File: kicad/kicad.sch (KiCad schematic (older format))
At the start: 10 parts, among them J1 Conn_ARM_JTAG_SWD_10, U1 ATSAMC21N18A-TQFP32

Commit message: Added the potentiometer to the schematic
Changed the schematic to reflect the use of the
ADC, PWM and potentiometer.
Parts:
- added RV1: 10K, symbol Device:R_POT
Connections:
- net GND: now also U1.6 (PA05), RV1.3
- net VCC: now also U1.4 (PA03), RV1.1
- net at U1.16 (PA15): now also D1.2 (A)
- net at U1.21 (PA22): no longer D1.2 (A)
- net at U1.3 (PA02): now also RV1.2
- no-connect marks 25 -> 22
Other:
- moved on the sheet: J1, R1
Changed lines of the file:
@@
 L Device:R R1
 U 1 1 5E23DDA0
-P 3900 2550
-F 0 "R1" H 3970 2596 50  0000 L CNN
-F 1 "1K" H 3970 2505 50  0000 L CNN
-F 2 "" V 3830 2550 50  0001 C CNN
-F 3 "~" H 3900 2550 50  0001 C CNN
-	1    3900 2550
-	1    0    0    -1
-$EndComp
-Wire Wire Line
-	3900 4500 4475 4500
+P 3500 2550
+F 0 "R1" H 3570 2596 50  0000 L CNN
+F 1 "1K" H 3570 2505 50  0000 L CNN
+F 2 "" V 3430 2550 50  0001 C CNN
+F 3 "~" H 3500 2550 50  0001 C CNN
+	1    3500 2550
+	1    0    0    -1
+$EndComp
+Wire Wire Line
+	3500 4500 4475 4500
 Connection ~ 5675 1975
 $Comp
@@
 $EndComp
 Wire Wire Line
-	3900 2400 3900 1975
-Wire Wire Line
-	3900 2700 3900 4200
-Wire Wire Line
-	2975 4000 3450 4000
-Wire Wire Line
-	3450 4000 3450 4600
-Wire Wire Line
-	3450 4600 4475 4600
-Wire Wire Line
-	2975 4200 3900 4200
-Connection ~ 3900 4200
-Wire Wire Line
-	3900 4200 3900 4500
-Wire Wire Line
-	4475 4400 3275 4400
-Wire Wire Line
-	3275 4400 3275 4300
-Wire Wire Line
-	3275 4300 2975 4300
-NoConn ~ 2975 4400
+	3500 2400 3500 1975
+Wire Wire Line
+	3500 2700 3500 4300
+Wire Wire Line
+	2975 4100 3175 4100
+Wire Wire Line
+	3175 4100 3175 4600
+Wire Wire Line
+	3175 4600 4475 4600
+Wire Wire Line
+	2975 4300 3500 4300
+Connection ~ 3500 4300
+Wire Wire Line
+	3500 4300 3500 4500
 NoConn ~ 2975 4500
+NoConn ~ 2975 4600
 $Comp
 L local_syms:Conn_ARM_JTAG_SWD_10 J1
 U 1 1 5E24CFFF
-P 2475 4300
-F 0 "J1" H 2525 5081 50  0000 C CNN
-F 1 "Conn_ARM_JTAG_SWD_10" H 2525 4990 50  0000 C CNN
-F 2 "" H 2475 4300 50  0001 C CNN
-F 3 "http://infocenter.arm.com/help/topic/com.arm.doc.ddi0314h/DDI0314H_coresight_components_trm.pdf" V 2125 3050 50  0001 C CNN
-	1    2475 4300
+P 2475 4400
+F 0 "J1" H 2525 5181 50  0000 C CNN
+F 1 "Conn_ARM_JTAG_SWD_10" H 2525 5090 50  0000 C CNN
+F 2 "" H 2475 4400 50  0001 C CNN
+F 3 "http://infocenter.arm.com/help/topic/com.arm.doc.ddi0314h/DDI0314H_coresight_components_trm.pdf" V 2125 3150 50  0001 C CNN
+	1    2475 4400
 	1    0    0    -1
 $EndComp
@@
 	5425 5050 5125 5050
 Wire Wire Line
-	2375 5050 2375 4900
-Wire Wire Line
-	2475 4900 2475 5050
+	2375 5050 2375 5000
+Wire Wire Line
+	2475 5000 2475 5050
 Connection ~ 2475 5050
 Wire Wire Line
 	2475 5050 2375 5050
 Wire Wire Line
-	2575 4900 2575 5050
+	2575 5000 2575 5050
 Connection ~ 2575 5050
 Wire Wire Line
@@
 Connection ~ 5125 5050
 Wire Wire Line
-	5125 5050 2575 5050
+	5125 5050 4325 5050
 $Comp
 L Device:LED D1
@@
 	0    -1   -1   0
 $EndComp
-Wire Wire Line
-	6475 4100 6950 4100
-Wire Wire Line
-	6950 4100 6950 4300
 Wire Wire Line
 	5675 1975 5675 2200
@@
 Connection ~ 5425 1975
 Wire Wire Line
-	5425 1975 3900 1975
+	5425 1975 4325 1975
 Wire Wire Line
 	5425 1975 5675 1975
@@
 	5675 2500 5675 2900
 Wire Wire Line
-	2475 1975 3900 1975
-Wire Wire Line
-	2475 1975 2475 3700
-Connection ~ 3900 1975
+	2475 1975 3500 1975
+Wire Wire Line
+	2475 1975 2475 3800
+Connection ~ 3500 1975
 $Comp
 L Device:C C5
@@
 NoConn ~ 4475 3300
 NoConn ~ 4475 3400
-NoConn ~ 4475 3500
-NoConn ~ 4475 3600
 NoConn ~ 4475 3700
-NoConn ~ 4475 3800
 NoConn ~ 4475 3900
 NoConn ~ 4475 4000
@@
 NoConn ~ 6475 3400
 NoConn ~ 6475 3500
-NoConn ~ 6475 3600
-NoConn ~ 6475 3700
 NoConn ~ 6475 3800
 NoConn ~ 6475 3900
@@
 NoConn ~ 6475 4500
 NoConn ~ 6475 4600
+NoConn ~ 6475 4100
+Wire Wire Line
+	2975 4400 4475 4400
+$Comp
+L Device:R_POT RV1
+U 1 1 5E28D798
+P 3975 3500
+F 0 "RV1" H 3906 3546 50  0000 R CNN
+F 1 "10K" H 3906 3455 50  0000 R CNN
+F 2 "" H 3975 3500 50  0001 C CNN
+F 3 "~" H 3975 3500 50  0001 C CNN
+	1    3975 3500
+	1    0    0    -1
+$EndComp
+Wire Wire Line
+	4125 3500 4475 3500
+Wire Wire Line
+	3975 3350 3975 1975
+Connection ~ 3975 1975
+Wire Wire Line
+	3975 1975 3500 1975
+Wire Wire Line
+	3975 3650 3975 5050
+Connection ~ 3975 5050
+Wire Wire Line
+	3975 5050 2575 5050
+Wire Wire Line
+	4475 3800 4325 3800
+Wire Wire Line
+	4325 3800 4325 5050
+Connection ~ 4325 5050
+Wire Wire Line
+	4325 5050 3975 5050
+Text Label 4325 4325 1    50   ~ 0
+MUXNEG_AIN5
+Wire Wire Line
+	4475 3600 4325 3600
+Wire Wire Line
+	4325 3600 4325 1975
+Connection ~ 4325 1975
+Wire Wire Line
+	4325 1975 3975 1975
+Text Label 4325 3325 1    50   ~ 0
+VREFP_AIN1
+Wire Wire Line
+	6950 3600 6475 3600
+Wire Wire Line
+	6950 3600 6950 4300
+NoConn ~ 6475 3700
 $EndSCHEMATC

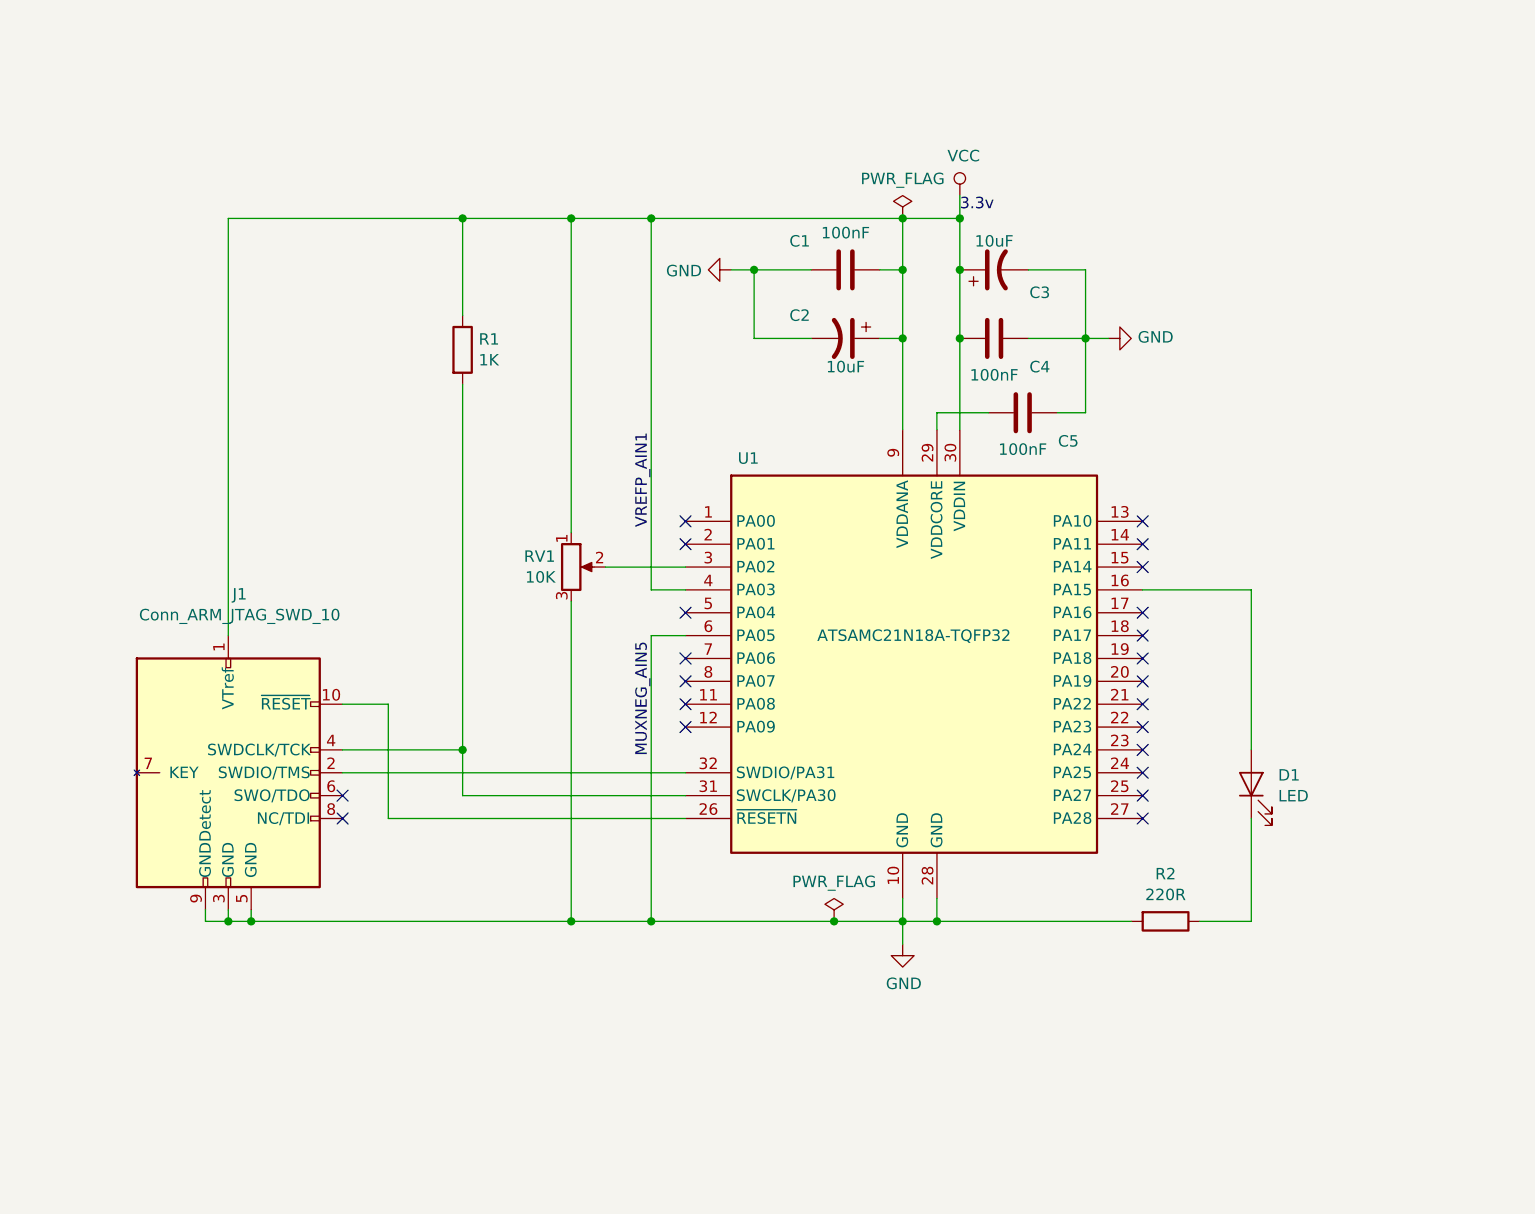
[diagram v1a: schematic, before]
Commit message: Added schematic for zero cross detector
Created a simple zero cross detector circuit using an optocoupler
and rectifier.
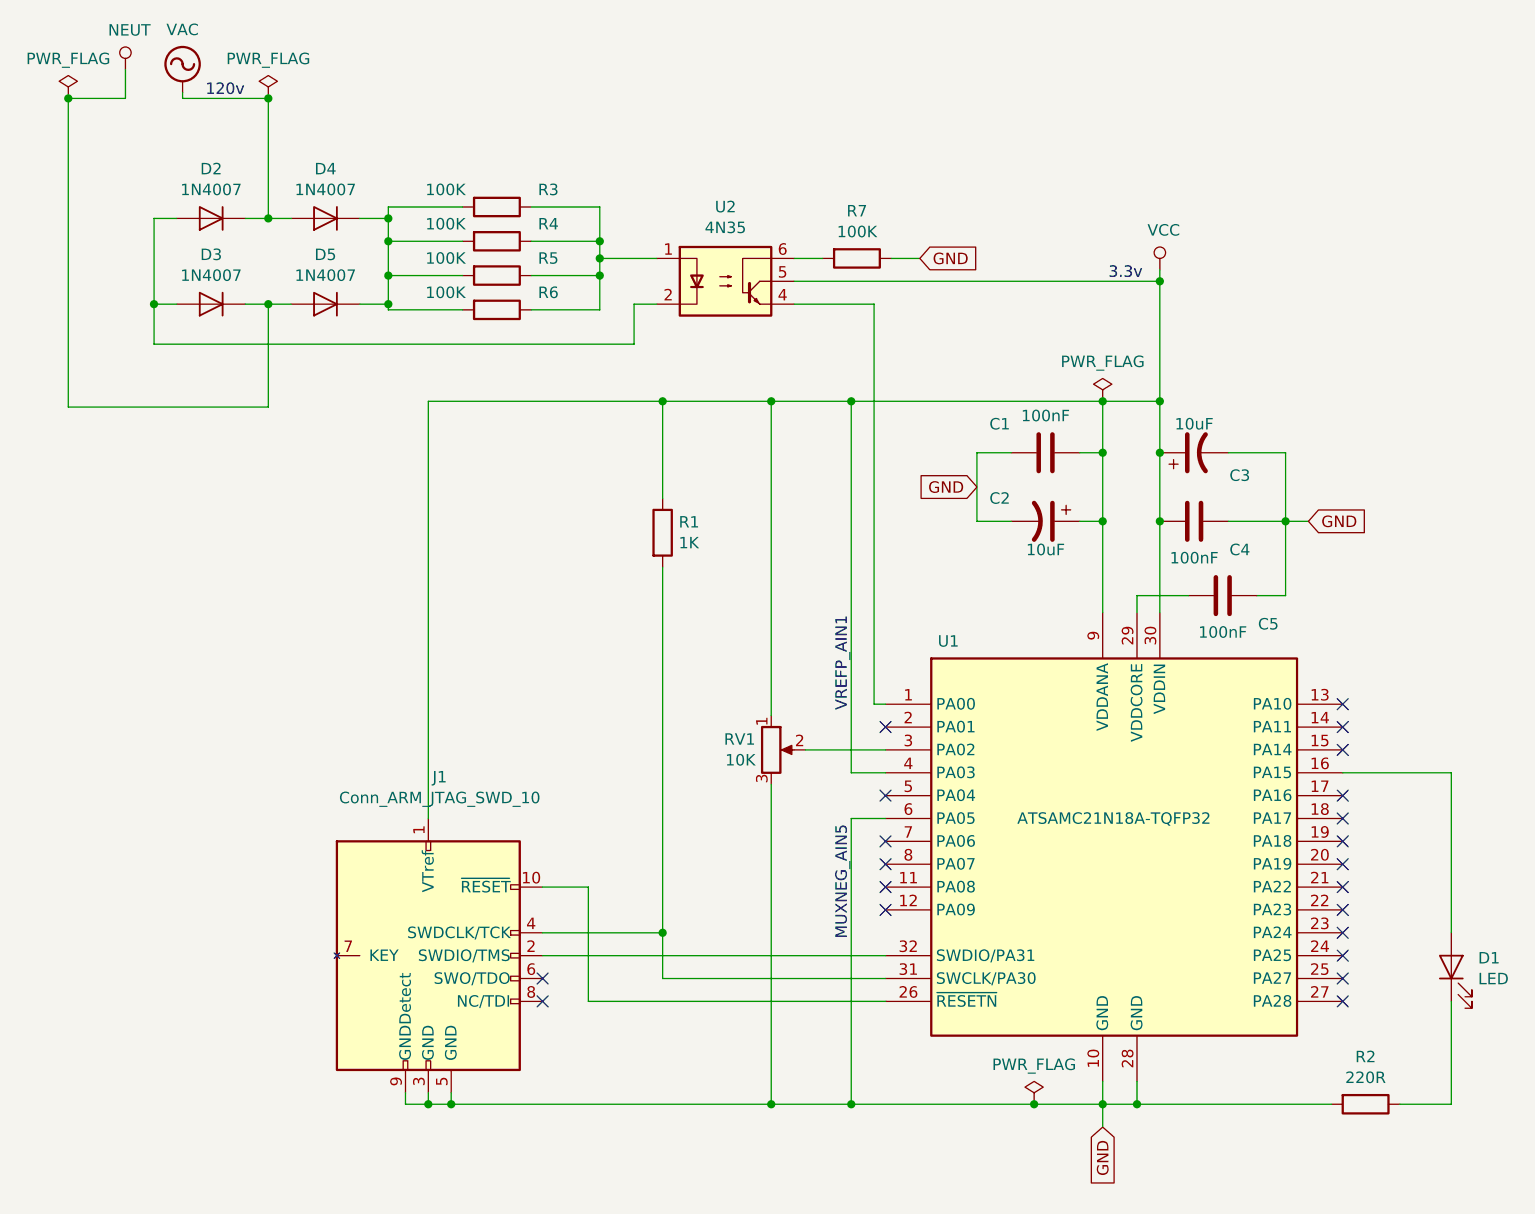
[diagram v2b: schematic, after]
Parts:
- added D2, D3, D4, D5: 1N4007, Diode_THT:D_DO-41_SOD81_P10.16mm_Horizontal, symbol Diode:1N4007
- added R3, R4, R5, R6, R7: 100K, symbol Device:R
- added U2: 4N35, Package_DIP:DIP-6_W7.62mm, symbol Isolator:4N35
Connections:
- net GND: now also R7.1
- net VCC: now also U2.5
- net at U1.1 (PA00): now also U2.4
- new net: R3.1, R4.1, R5.1, R6.1, U2.1
- new net: D2.2 (A), D3.2 (A), U2.2
- new net: R7.2, U2.6
- new net: D4.1 (K), D5.1 (K), R3.2, R4.2, R5.2, R6.2
- new net NEUT: D3.1 (K), D5.2 (A)
- new net VAC: D2.1 (K), D4.2 (A)
- no-connect marks 22 -> 21
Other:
- moved on the sheet: C1, C2, C3, C4, C5, D1, J1, R1, R2, RV1, U1
